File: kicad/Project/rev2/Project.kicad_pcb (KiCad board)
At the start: 4 copper layers, 99 x 98 mm, 88 parts, among them J1 USB_B_Micro, J2 SWD_Connector, J3 Micro_SD_Card_Det1, J4 01x10, J5 02x02, P1 S2B-PH-SM4-TB, Q1 DMP2070UQ, Q2 BC817, SW1 KMR2, U1 AP2112K-3.3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

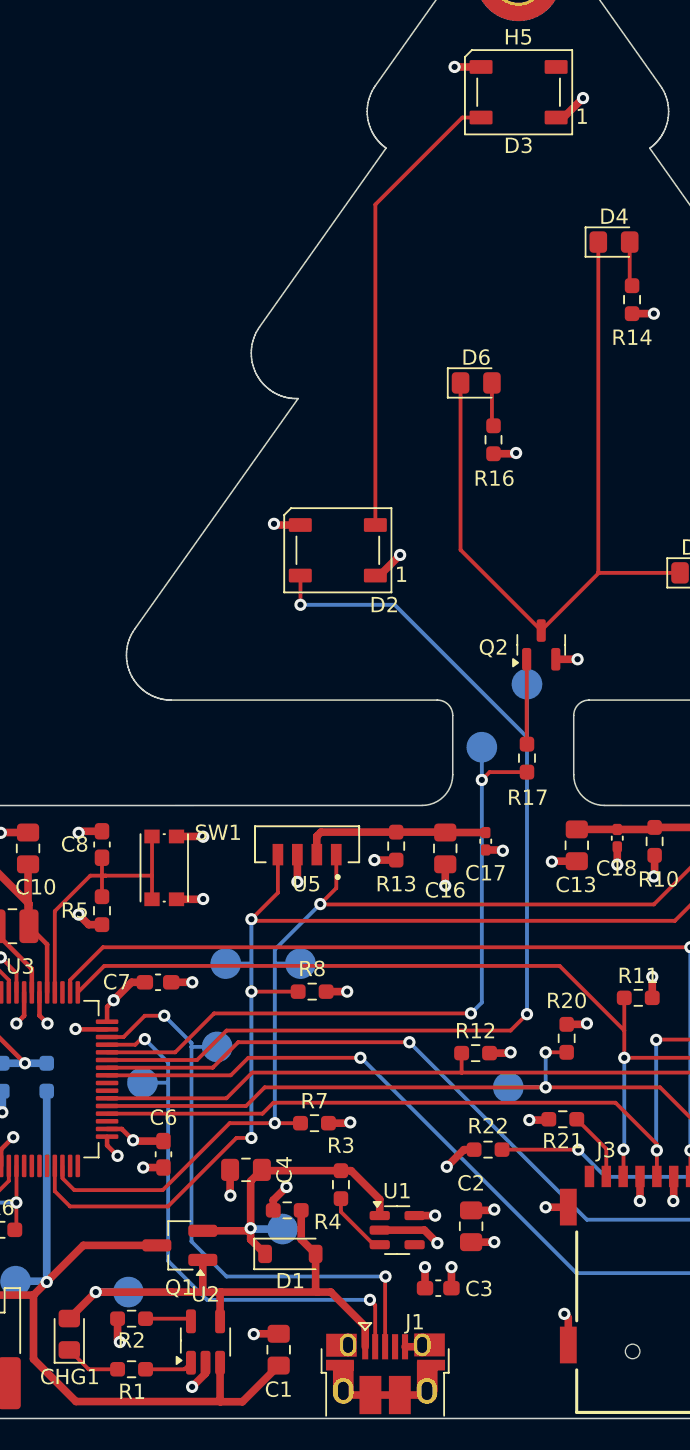
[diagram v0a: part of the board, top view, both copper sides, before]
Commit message: Add discovered errata
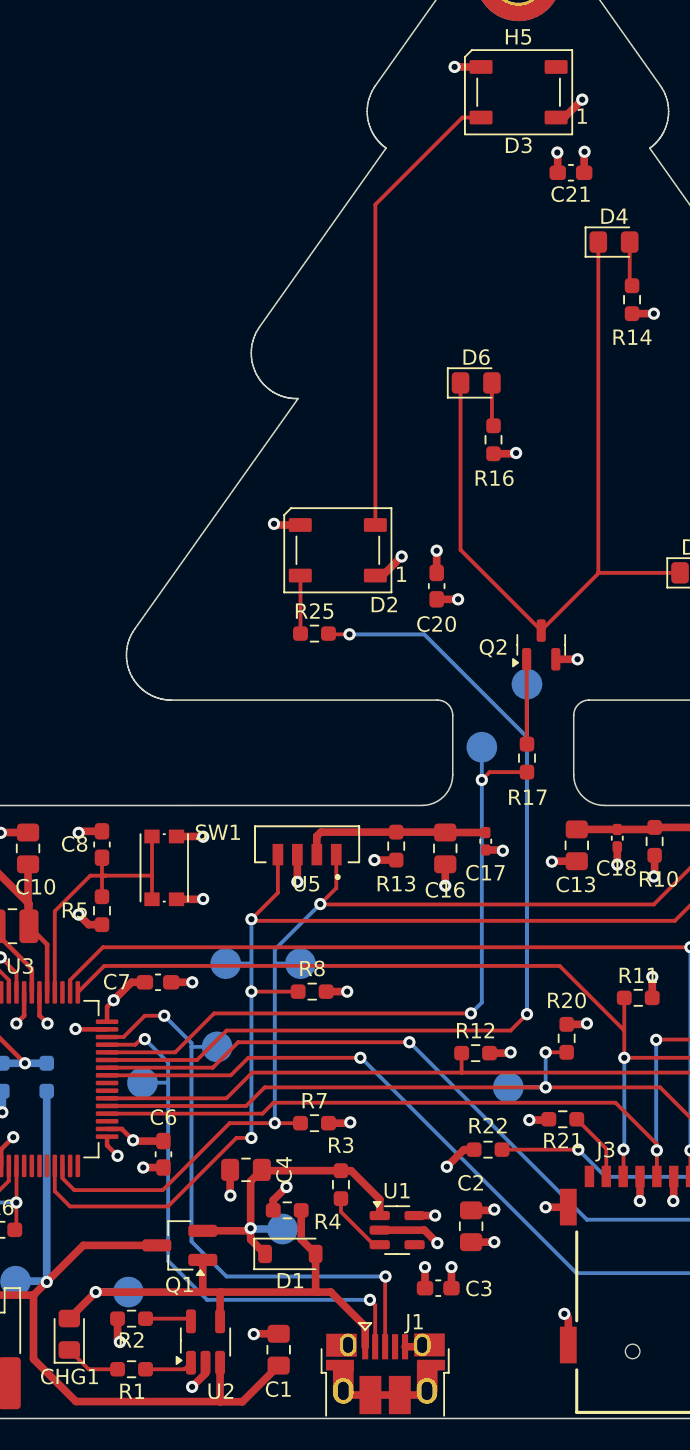
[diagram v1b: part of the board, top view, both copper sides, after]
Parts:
- added C20: 1uF, Capacitor_SMD:C_0603_1608Metric_Pad1.08x0.95mm_HandSolder, F.Cu at (222.0, 112.7)
- added C21: 1uF, Capacitor_SMD:C_0603_1608Metric_Pad1.08x0.95mm_HandSolder, F.Cu at (230.8, 85.7)
- added R25: 470R, Resistor_SMD:R_0603_1608Metric_Pad0.98x0.95mm_HandSolder, F.Cu at (214.0, 115.8)
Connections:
- D2 pad 4: /NEOPIXEL_CTRL -> /NEOPIXEL_CTRL_FILTERED
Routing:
- net /NEOPIXEL_CTRL: track 70.7 -> 66.1 mm
- net /NEOPIXEL_CTRL_FILTERED: track 0.00 -> 3.77 mm
- net GND: track 84.5 -> 87.3 mm, vias 44 -> 46
- net +3V3: track 62.1 -> 64.7 mm, vias 35 -> 37

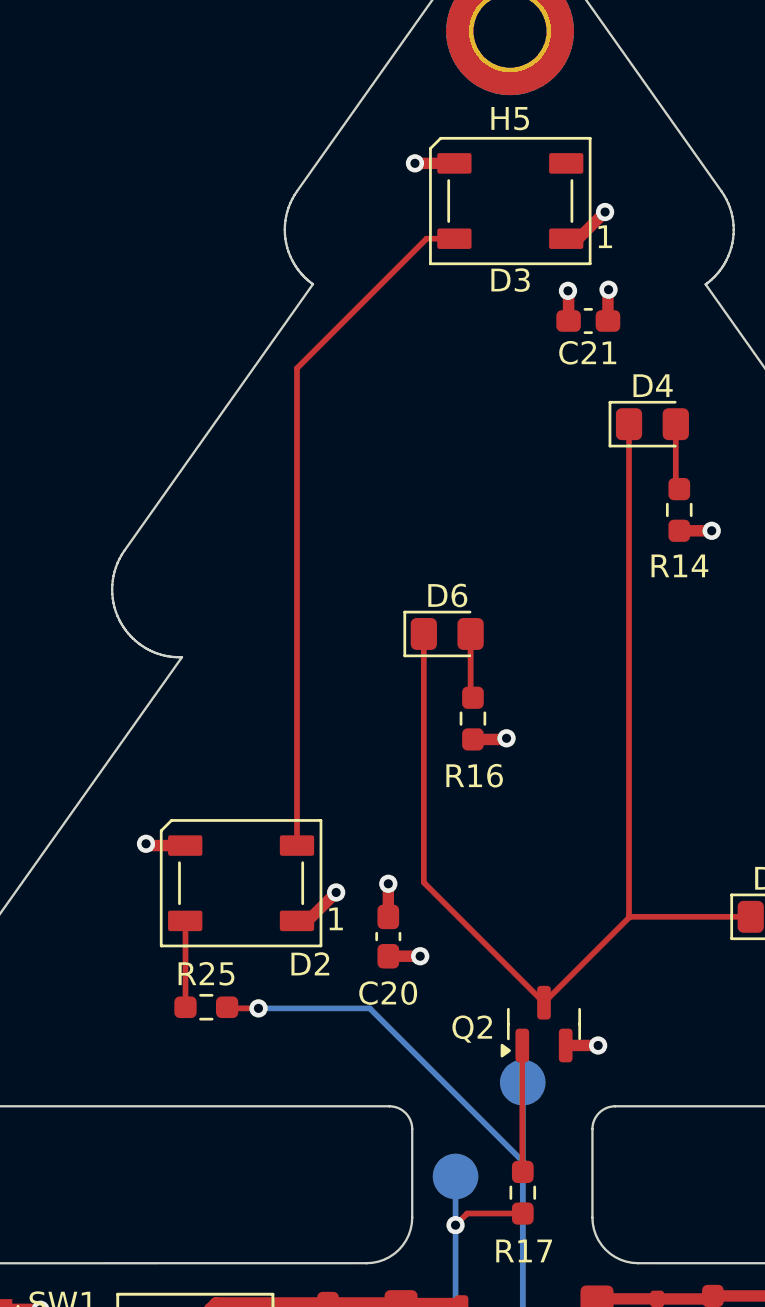
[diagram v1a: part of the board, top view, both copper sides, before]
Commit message: Use the more common NeoPixels
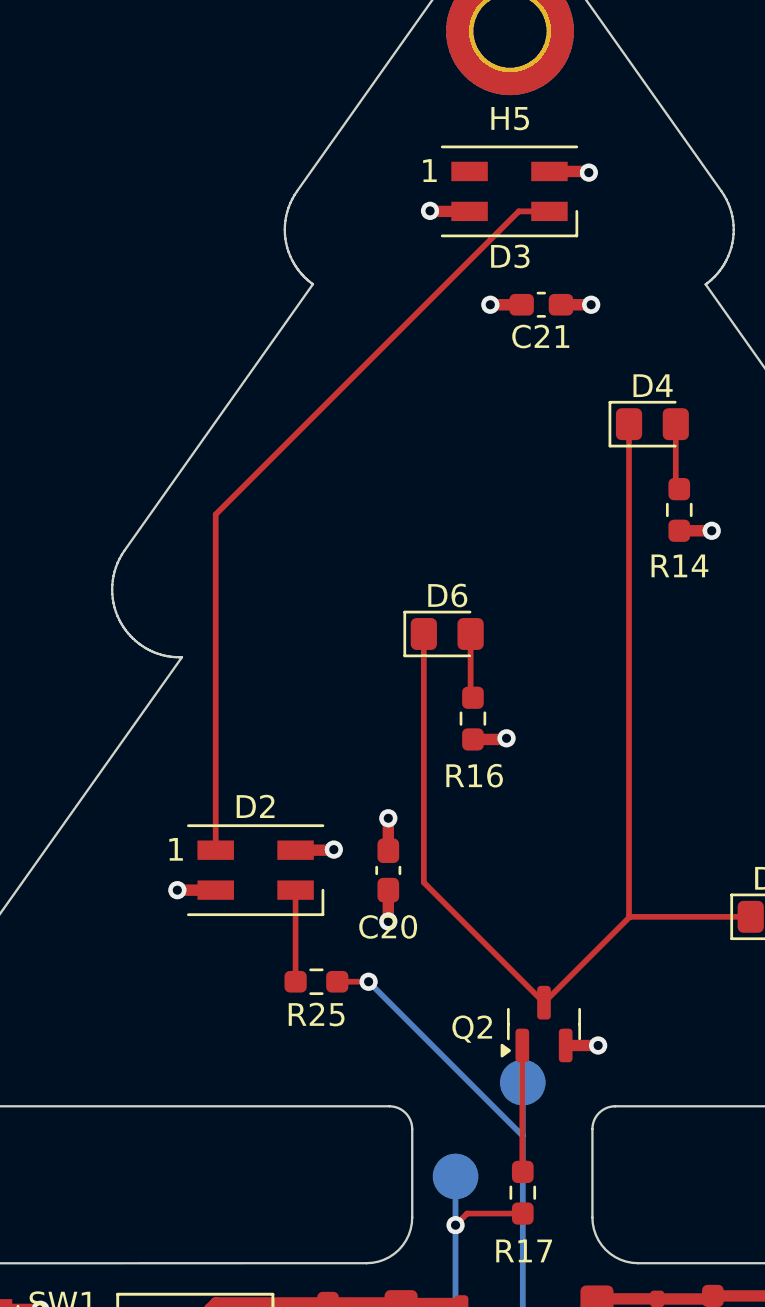
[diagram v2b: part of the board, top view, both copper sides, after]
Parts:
- D2, D3: value WS2812B -> SK6812MINI; footprint LED_SMD:LED_WS2812B_PLCC4_5.0x5.0mm_P3.2mm -> LED_SMD:LED_SK6812MINI_PLCC4_3.5x3.5mm_P1.75mm
- moved R25 4.95 mm to (218.8, 114.7)
- moved C20 2.90 mm to (222.0, 109.8)
- moved C21 2.18 mm to (228.7, 85.0)
- moved D2 0.86 mm to (216.2, 109.8), turned to 0 degrees
- moved D3 0.42 mm to (227.3, 80.0), turned to 0 degrees
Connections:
- D2 pad 1: +3V3 -> Net-(D2-DOUT)
- D2 pad 2: Net-(D2-DOUT) -> GND
- D2 pad 3: GND -> /NEOPIXEL_CTRL_FILTERED
- D2 pad 4: /NEOPIXEL_CTRL_FILTERED -> +3V3
- D3 pad 1: +3V3 -> unconnected-(D3-DOUT-Pad1)
- D3 pad 2: unconnected-(D3-DOUT-Pad2) -> GND
- D3 pad 3: GND -> Net-(D2-DOUT)
- D3 pad 4: Net-(D2-DOUT) -> +3V3
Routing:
- net /NEOPIXEL_CTRL: track 66.1 -> 61.1 mm
- net Net-(D2-DOUT): track 30.2 -> 34.8 mm
